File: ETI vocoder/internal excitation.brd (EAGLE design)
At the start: 160 x 100 mm, 49 parts, among them IC1 LM1458N, IC3 TL081P, IC4 UA741P, IC5 4006N, IC6 4030N, IC7 LM1458N, Q1 BC182L

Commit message: All ETI boards checked for caps and pots
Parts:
- removed C3: (no value), resistor:E2,5-5
- removed CARD2: (no value), con-molex:22-23-2061
- removed R10: 1k, resistor:0207/7
- added BOARD1: 22-23-2041, con-molex:22-23-2041
- added BOARD1-PWR: 22-23-2021, con-molex:22-23-2021
- added C9: 10u, resistor:E2,5-5
- added R49: 1k, resistor:0207/7
- C1, C8: device resistor:C050-025X075 -> resistor:C075-032X103
- C6: device resistor:C025-025X050 -> resistor:C075-032X103
- moved R19 198.2 mm to (108.0, 33.7), turned to 180 degrees
- moved Q1 182.0 mm to (92.7, 33.0)
- moved C6 169.3 mm to (104.8, 11.4), turned to 180 degrees
- moved RV7 167.2 mm to (102.9, 3.81)
- moved R26 166.7 mm to (65.4, 21.6), turned to 270 degrees
- moved R23 165.9 mm to (87.6, 10.2)
- moved R25 163.5 mm to (71.8, 21.6), turned to 270 degrees
- moved IC6 162.9 mm to (86.4, 21.6)
- moved C7 161.9 mm to (87.6, 6.99), turned to 180 degrees
- moved IC5 161.6 mm to (105.4, 21.6)
- moved D4 161.3 mm to (65.4, 34.3), turned to 180 degrees
- moved C5 156.7 mm to (97.2, 12.1), turned to 270 degrees
- moved R22 155.8 mm to (87.6, 13.3)
- moved D2 153.0 mm to (71.8, 27.9)
- moved D3 144.9 mm to (54.0, 27.9)
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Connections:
- removed net N$14 (its old number): IC4.2, R17.2, R8.1, RV7.1S
- net +12V: now also R49.2; no longer R10.2
- net BOARD2_MIX: now also BOARD1.4, IC4.2, R17.2, R8.1, RV7.1S; no longer CARD2.4
- net GND: now also C9.-, RV5.1E, RV7.1A; no longer C3.-, RV5.1A, RV7.1E
- net N$9: now also RV5.1A; no longer RV5.1E
- net VCA_CTRL: now also BOARD1.2; no longer CARD2.2
- net VCA_SIGNAL: now also BOARD1.3, RV7.1E; no longer CARD2.1, RV7.1A
- net VDD: now also BOARD1-PWR.2, C9.+, R49.1; no longer C3.+, CARD2.5, R10.1
- net VSS: now also BOARD1-PWR.1; no longer CARD2.6
- net X: now also BOARD1.1; no longer CARD2.3
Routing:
- net GND: track 0.00 -> 266.1 mm, vias 0 -> 1
- net +12V: track 0.00 -> 114.5 mm
- net BOARD2_MIX: track 0.00 -> 111.5 mm
- net VSS: track 0.00 -> 108.5 mm
- net VDD: track 0.00 -> 107.9 mm
- net -12V: track 0.00 -> 93.2 mm
- net VCA_SIGNAL: track 0.00 -> 62.1 mm
- net X: track 0.00 -> 48.7 mm
- net N$26: track 0.00 -> 44.1 mm
- net 5_9: track 0.00 -> 42.9 mm
- net N$10: track 0.00 -> 35.3 mm
- net N$6: track 0.00 -> 35.2 mm
- net N$32: track 0.00 -> 30.3 mm
- net N$15: track 0.00 -> 28.2 mm
- net 4_10: track 0.00 -> 25.5 mm
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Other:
- board size 160 x 100 mm -> 114.9 x 38.4 mm
- board text added: "+12V"
- board text added: "+7V"
- board text added: "-12V"
- board text added: "-7V"
- board text added: "4V&B"
- board text added: "Ctrl"
- board text added: "ETI Vocoder"
- board text added: "GND"
- board text added: "Int Excitation"
- board text added: "Mix"
- board text added: "Sig"
- board text added: "Upper board v1.0"
- board text added: "X"

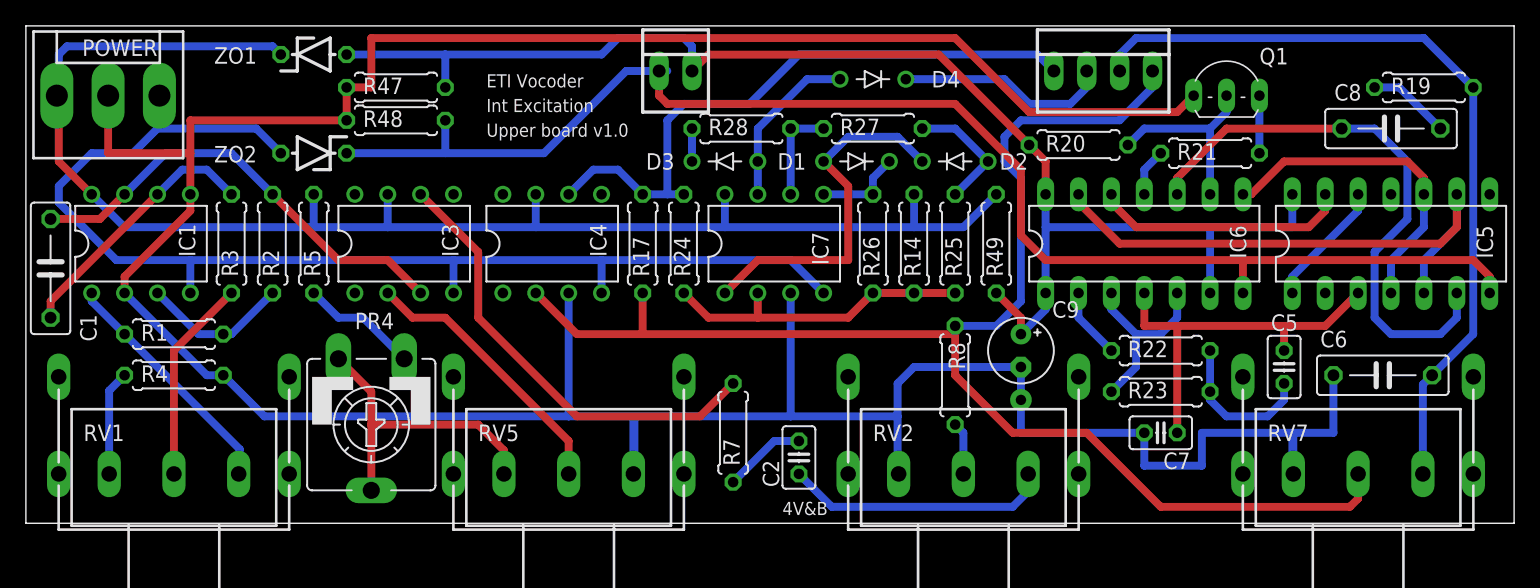
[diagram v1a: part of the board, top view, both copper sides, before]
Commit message: Fixed input boards in regards to article and added spacer holes
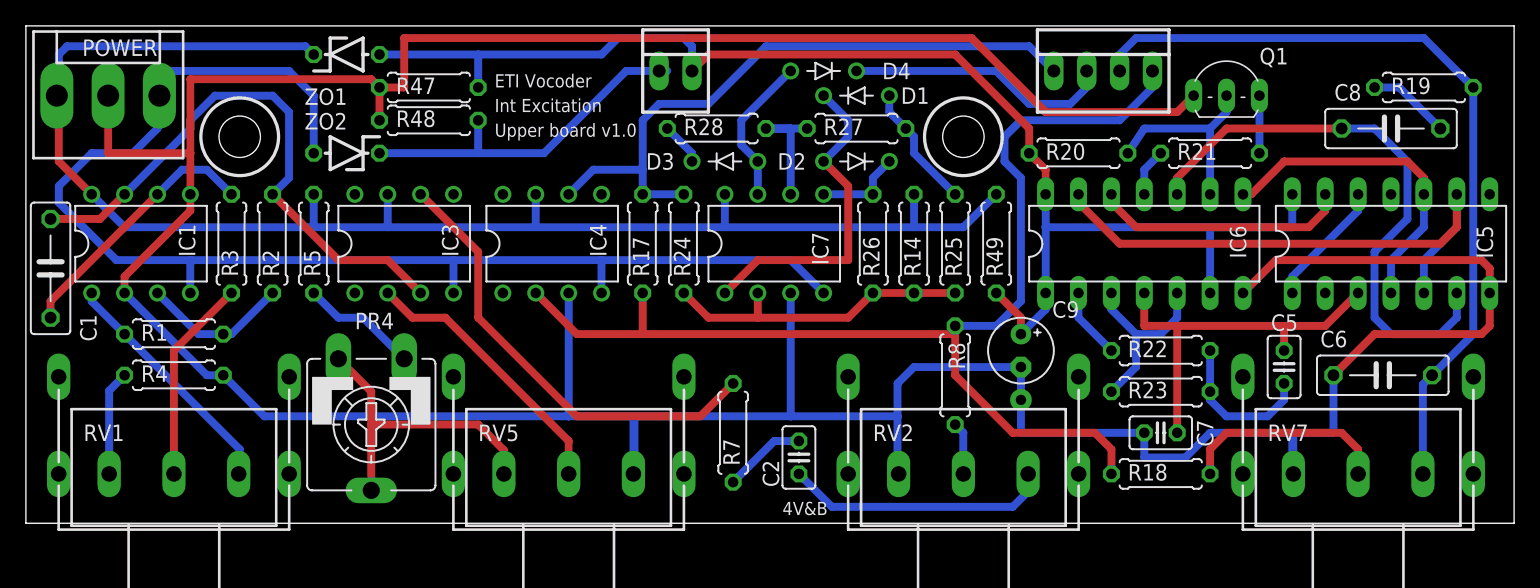
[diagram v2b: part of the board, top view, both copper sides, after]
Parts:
- added R18: 47k, resistor:0207/7
- C2: value 100n -> 10n
- C6: value 100n -> 33n
- R49: value 1k -> 3k3
- moved D2 7.62 mm to (64.1, 27.9), turned to 180 degrees
- moved D1 5.08 mm to (64.1, 33.0), turned to 0 degrees
- moved D4 3.86 mm to (61.6, 34.9)
- moved R47 2.54 mm to (31.1, 33.7)
- moved R48 2.54 mm to (31.1, 31.1)
- moved ZO1 2.54 mm to (24.8, 36.2)
- moved ZO2 2.54 mm to (24.8, 28.6)
- moved R28 1.90 mm to (53.3, 30.5)
- moved R27 1.27 mm to (64.1, 30.5)
- moved R20 0.64 mm to (81.3, 28.6)
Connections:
- new net N$22: R18.2, RV7.1S
- net BOARD2_MIX: now also R18.1; no longer RV7.1S
- net GND: now also IC5.7, IC6.7
- net N$15: now also D1.C, D2.A; no longer D1.A, D2.C
- net N$17: now also D2.C; no longer D1.C
- net N$18: now also D1.A; no longer D2.A
- net VSS: no longer IC5.7, IC6.7
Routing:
- net VSS: track 108.5 -> 27.4 mm
- net GND: track 266.1 -> 305.6 mm
- net BOARD2_MIX: track 111.5 -> 90.4 mm
- net N$22: track 0.00 -> 16.3 mm
- net N$6: track 35.2 -> 44.7 mm
- net -12V: track 93.2 -> 102.3 mm
- net VCA_CTRL: track 16.6 -> 20.6 mm
- net +12V: track 114.5 -> 117.0 mm
- net N$19: track 7.62 -> 10.2 mm
- net N$15: track 28.2 -> 25.6 mm
- net VDD: track 107.9 -> 106.1 mm
- net X: track 48.7 -> 50.3 mm
- net N$21: track 13.0 -> 11.6 mm
- net N$20: track 2.54 -> 3.33 mm

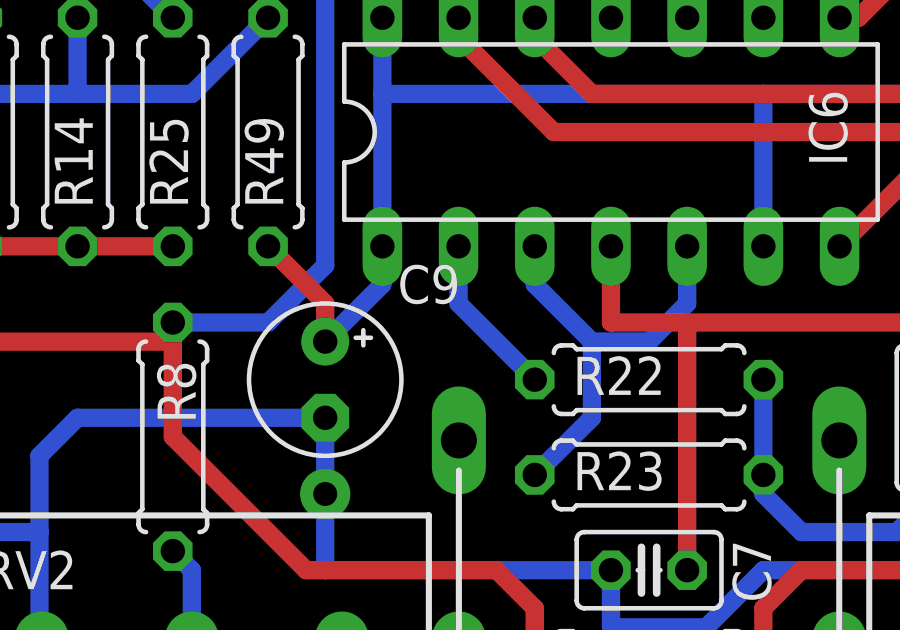
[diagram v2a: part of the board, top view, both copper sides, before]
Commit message: Finished first of two halves of the universal voice board
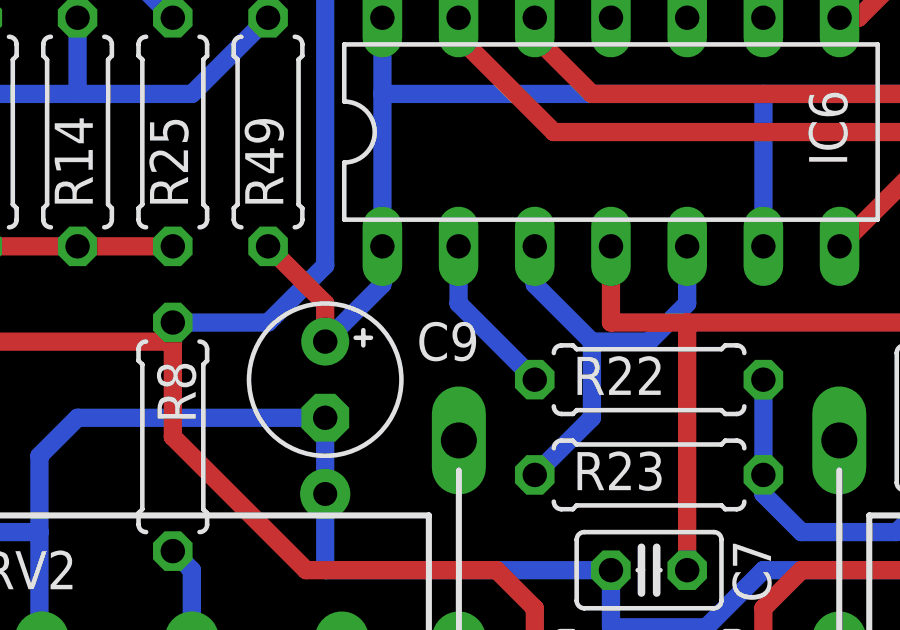
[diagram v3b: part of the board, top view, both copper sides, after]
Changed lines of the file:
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@@
 </element>
 <element name="C9" library="resistor" package="E2,5-5" value="10u" x="76.835" y="13.335" smashed="yes" rot="R270">
-<attribute name="NAME" x="79.248" y="15.875" size="1.27" layer="25" ratio="10"/>
+<attribute name="NAME" x="79.883" y="13.97" size="1.27" layer="25" ratio="10"/>
 <attribute name="VALUE" x="74.422" y="10.922" size="1.27" layer="27" ratio="10" rot="R270"/>
 </element>
